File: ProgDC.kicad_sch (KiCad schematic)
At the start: 45 parts, among them J1 Conn_02x20_Counter_Clockwise_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, J2 Conn_01x24_Pin, J3 Conn_01x03_Pin, U1 KR580VK28, U2 628512, U3 CPU

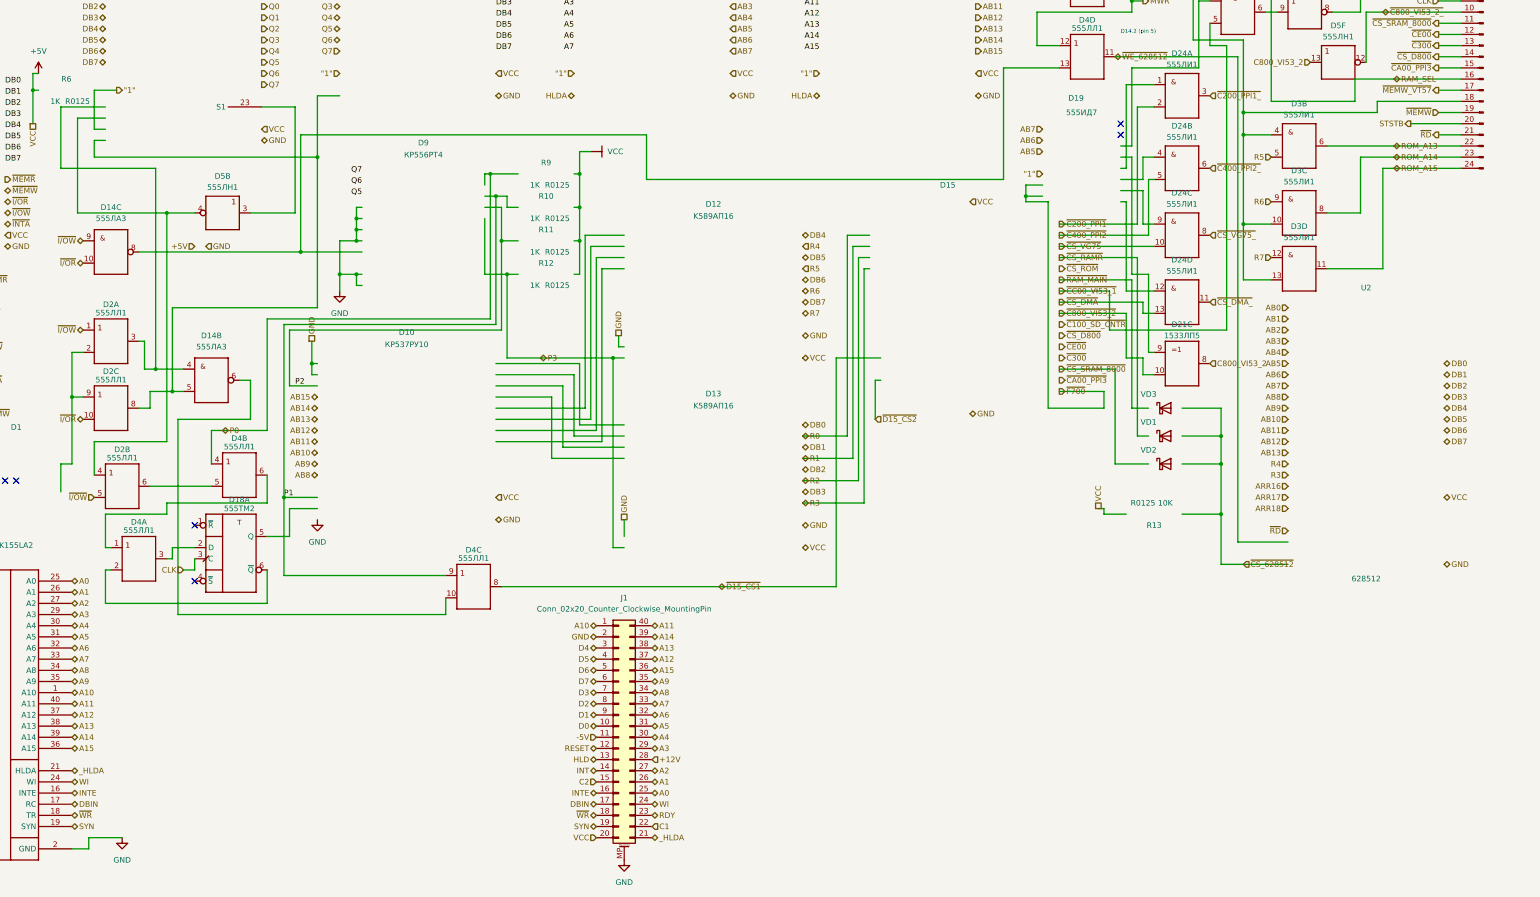
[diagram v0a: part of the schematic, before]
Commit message: Fix address and data buffering
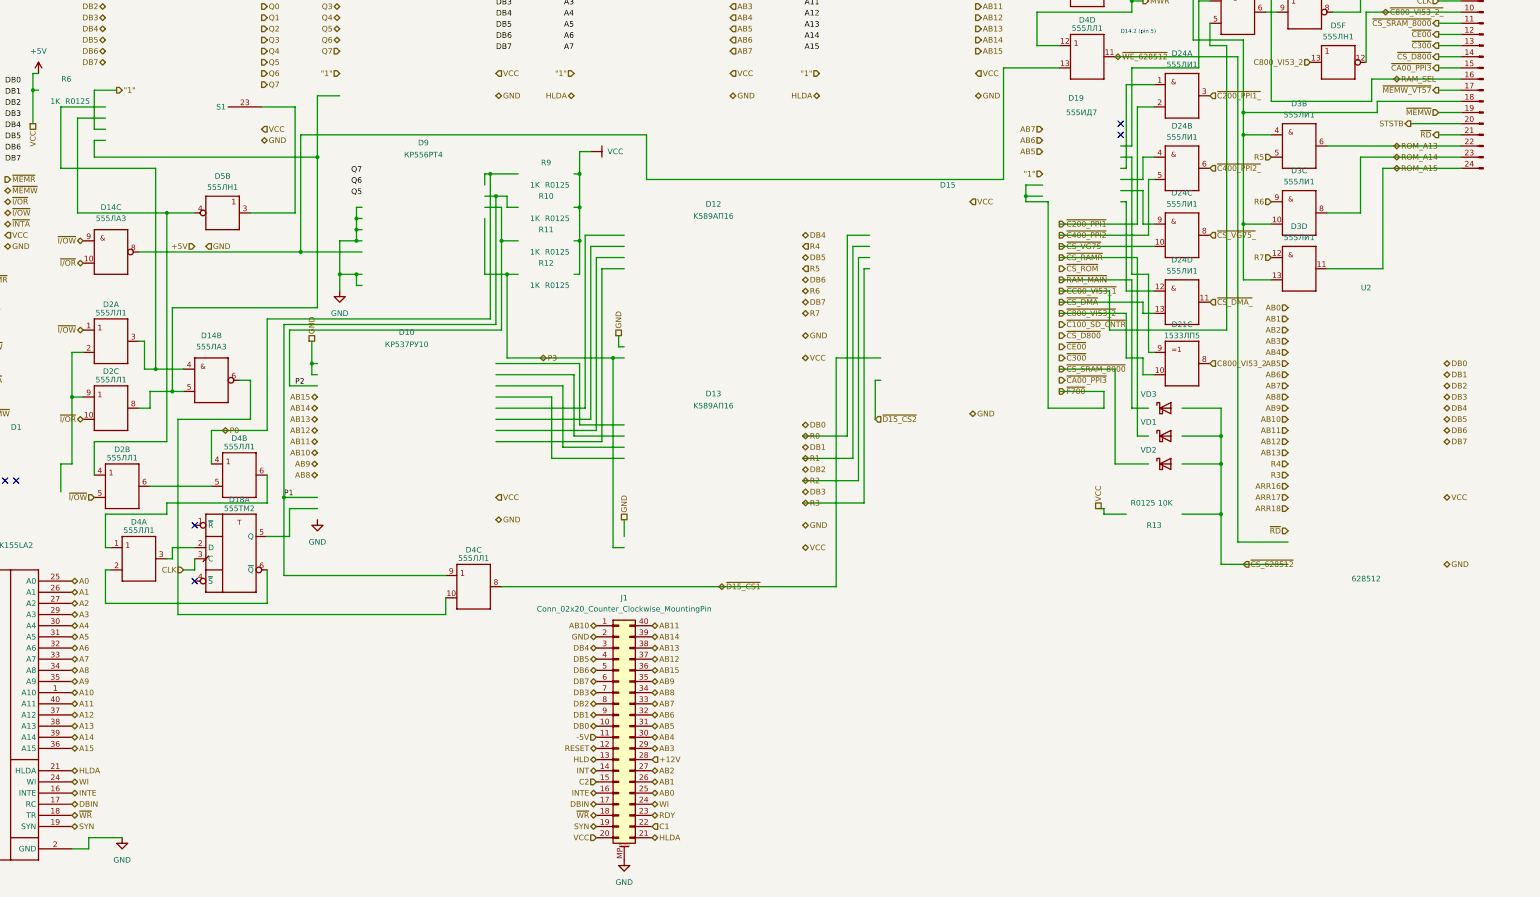
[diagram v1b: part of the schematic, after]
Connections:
- net _HLDA is gone; now on net HLDA: J1.21 (Pin_21), U3.21 (HLDA)
- net A0: no longer J1.25 (Pin_25)
- net A1: no longer J1.26 (Pin_26)
- net A10: no longer J1.1 (Pin_1)
- net A11: no longer J1.40 (Pin_40)
- net A12: no longer J1.37 (Pin_37)
- net A13: no longer J1.38 (Pin_38)
- net A14: no longer J1.39 (Pin_39)
- net A15: no longer J1.36 (Pin_36)
- net A2: no longer J1.27 (Pin_27)
- net A3: no longer J1.29 (Pin_29)
- net A4: no longer J1.30 (Pin_30)
- net A5: no longer J1.31 (Pin_31)
- net A6: no longer J1.32 (Pin_32)
- net A7: no longer J1.33 (Pin_33)
- net A8: no longer J1.34 (Pin_34)
- net A9: no longer J1.35 (Pin_35)
- net AB0: now also J1.25 (Pin_25)
- net AB1: now also J1.26 (Pin_26)
- net AB10: now also J1.1 (Pin_1)
- net AB11: now also J1.40 (Pin_40)
- net AB12: now also J1.37 (Pin_37)
- net AB13: now also J1.38 (Pin_38)
- net AB14: now also J1.39 (Pin_39)
- net AB15: now also J1.36 (Pin_36)
- net AB2: now also J1.27 (Pin_27)
- net AB3: now also J1.29 (Pin_29)
- net AB4: now also J1.30 (Pin_30)
- net AB5: now also J1.31 (Pin_31)
- net AB6: now also J1.32 (Pin_32)
- net AB7: now also J1.33 (Pin_33)
- net AB8: now also J1.34 (Pin_34)
- net AB9: now also J1.35 (Pin_35)
- net D0: no longer J1.10 (Pin_10)
- net D1: no longer J1.9 (Pin_9)
- net D2: no longer J1.8 (Pin_8)
- net D3: no longer J1.7 (Pin_7)
- net D4: no longer J1.3 (Pin_3)
- net D5: no longer J1.4 (Pin_4)
- net D6: no longer J1.5 (Pin_5)
- net D7: no longer J1.6 (Pin_6)
- net DB0: now also J1.10 (Pin_10)
- net DB1: now also J1.9 (Pin_9)
- net DB2: now also J1.8 (Pin_8)
- net DB3: now also J1.7 (Pin_7)
- net DB4: now also J1.3 (Pin_3)
- net DB5: now also J1.4 (Pin_4)
- net DB6: now also J1.5 (Pin_5)
- net DB7: now also J1.6 (Pin_6)
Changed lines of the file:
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@@
 	(wire
 		(pts
-			(xy 375.92 109.22) (xy 375.92 104.14)
+			(xy 379.73 109.22) (xy 379.73 104.14)
 		)
 		(stroke
@@
 	(wire
 		(pts
-			(xy 375.92 104.14) (xy 400.05 104.14)
+			(xy 379.73 104.14) (xy 400.05 104.14)
 		)
 		(stroke
@@
 	(wire
 		(pts
-			(xy 356.87 109.22) (xy 375.92 109.22)
+			(xy 356.87 109.22) (xy 379.73 109.22)
 		)
 		(stroke
@@
 		)
 	)
-	(hierarchical_label "_HLDA"
+	(hierarchical_label "HLDA"
 		(shape bidirectional)
 		(at 83.82 261.62 0)
@@
 				(size 1.27 1.27)
 			)
-			(justify left)
+			(justify left bottom)
 		)
 	)
@@
 		)
 	)
-	(hierarchical_label "D4"
+	(hierarchical_label "DB4"
 		(shape bidirectional)
 		(at 203.2 233.68 180)
@@
 				(size 1.27 1.27)
 			)
-			(justify left)
+			(justify left bottom)
 		)
 	)
@@
 		)
 	)
-	(hierarchical_label "A0"
+	(hierarchical_label "AB0"
 		(shape bidirectional)
 		(at 215.9 266.7 0)
@@
 				(size 1.27 1.27)
 			)
-			(justify left)
+			(justify left bottom)
 		)
 	)
@@
 		)
 	)
-	(hierarchical_label "A10"
+	(hierarchical_label "AB10"
 		(shape bidirectional)
 		(at 203.2 228.6 180)
@@
 		)
 	)
-	(hierarchical_label "D6"
+	(hierarchical_label "DB6"
 		(shape bidirectional)
 		(at 203.2 238.76 180)
@@
 		)
 	)
-	(hierarchical_label "_HLDA"
+	(hierarchical_label "HLDA"
 		(shape bidirectional)
 		(at 215.9 276.86 0)
@@
 		)
 	)
-	(hierarchical_label "D5"
+	(hierarchical_label "DB5"
 		(shape bidirectional)
 		(at 203.2 236.22 180)
@@
 				(size 1.27 1.27)
 			)
-			(justify left)
+			(justify left bottom)
 		)
 	)
@@
 				(size 1.27 1.27)
 			)
-			(justify left)
+			(justify left bottom)
 		)
 	)
@@
 		)
 	)
-	(hierarchical_label "A13"
+	(hierarchical_label "AB13"
 		(shape bidirectional)
 		(at 215.9 233.68 0)
@@
 				(size 1.27 1.27)
 			)
-			(justify left)
+			(justify left bottom)
 		)
 	)
@@
 		)
 	)
-	(hierarchical_label "D0"
+	(hierarchical_label "DB0"
 		(shape bidirectional)
 		(at 203.2 251.46 180)
@@
 		)
 	)
-	(hierarchical_label "A14"
+	(hierarchical_label "AB14"
 		(shape bidirectional)
 		(at 215.9 231.14 0)
@@
 		)
 	)
-	(hierarchical_label "A9"
+	(hierarchical_label "AB9"
 		(shape bidirectional)
 		(at 215.9 241.3 0)
@@
 		)
 	)
-	(hierarchical_label "A5"
+	(hierarchical_label "AB5"
 		(shape bidirectional)
 		(at 215.9 251.46 0)
@@
 				(size 1.27 1.27)
 			)
-			(justify left)
+			(justify left bottom)
 		)
 	)
-	(hierarchical_label "D7"
+	(hierarchical_label "DB7"
 		(shape bidirectional)
 		(at 203.2 241.3 180)
@@
 				(size 1.27 1.27)
 			)
-			(justify left)
+			(justify left bottom)
 		)
 	)
@@
 		)
 	)
-	(hierarchical_label "A4"
+	(hierarchical_label "AB4"
 		(shape bidirectional)
 		(at 215.9 254 0)
@@
 		)
 	)
-	(hierarchical_label "A1"
+	(hierarchical_label "AB1"
 		(shape bidirectional)
 		(at 215.9 264.16 0)
@@
 				(size 1.27 1.27)
 			)
-			(justify left)
+			(justify left bottom)
 		)
 	)
@@
 				(size 1.27 1.27)
 			)
-			(justify left)
+			(justify left bottom)
 		)
 	)
@@
 		)
 	)
-	(hierarchical_label "D1"
+	(hierarchical_label "DB1"
 		(shape bidirectional)
 		(at 203.2 248.92 180)
@@
 		)
 	)
-	(hierarchical_label "A15"
+	(hierarchical_label "AB15"
 		(shape bidirectional)
 		(at 215.9 238.76 0)
@@
 				(size 1.27 1.27)
 			)
-			(justify left)
+			(justify left bottom)
 		)
 	)
@@
 				(size 1.27 1.27)
 			)
-			(justify left)
+			(justify left bottom)
 		)
 	)
@@
 				(size 1.27 1.27)
 			)
-			(justify left)
+			(justify left bottom)
 		)
 	)
@@
 		)
 	)
-	(hierarchical_label "A7"
+	(hierarchical_label "AB7"
 		(shape bidirectional)
 		(at 215.9 246.38 0)
@@
 				(size 1.27 1.27)
 			)
-			(justify left)
+			(justify left bottom)
 		)
 	)
@@
 				(size 1.27 1.27)
 			)
-			(justify left)
+			(justify left bottom)
 		)
 	)
@@
 		)
 	)
-	(hierarchical_label "A2"
+	(hierarchical_label "AB2"
 		(shape bidirectional)
 		(at 215.9 261.62 0)
@@
 		)
 	)
-	(hierarchical_label "A3"
+	(hierarchical_label "AB3"
 		(shape bidirectional)
 		(at 215.9 256.54 0)
@@
 		)
 	)
-	(hierarchical_label "A6"
+	(hierarchical_label "AB6"
 		(shape bidirectional)
 		(at 215.9 248.92 0)
@@
 				(size 1.27 1.27)
 			)
-			(justify left)
+			(justify left bottom)
 		)
 	)
@@
 		)
 	)
-	(hierarchical_label "A11"
+	(hierarchical_label "AB11"
 		(shape bidirectional)
 		(at 215.9 228.6 0)
@@
 				(size 1.27 1.27)
 			)
-			(justify left)
+			(justify left bottom)
 		)
 	)
@@
 		)
 	)
-	(hierarchical_label "A8"
+	(hierarchical_label "AB8"
 		(shape bidirectional)
 		(at 215.9 243.84 0)
@@
 		)
 	)
-	(hierarchical_label "D3"
+	(hierarchical_label "DB3"
 		(shape bidirectional)
 		(at 203.2 243.84 180)
@@
 				(size 1.27 1.27)
 			)
-			(justify left)
+			(justify left bottom)
 		)
 	)
@@
 		)
 	)
-	(hierarchical_label "D2"
+	(hierarchical_label "DB2"
 		(shape bidirectional)
 		(at 203.2 246.38 180)
@@
 				(size 1.27 1.27)
 			)
-			(justify right)
+			(justify right bottom)
 		)
 	)
@@
 		)
 	)
-	(hierarchical_label "A12"
+	(hierarchical_label "AB12"
 		(shape bidirectional)
 		(at 215.9 236.22 0)

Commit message: Ver. 1.4
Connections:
- net ~{CS_DMA_}: now also D22.9 (A); no longer J2.8 (Pin_8)
- net ~{CS_RAMR}: now also D22.5 (A)
- net ~{WR}: now also D22.1 (A)
- net ~{CS_DMA_2}: now reaches D21.11 (Y)
- net ~{CS_DMA_2}: now also J2.8 (Pin_8)
- net at D21.12 (A): now also D22.8 (Y)
- net at D21.13 (B): now also D14.11 (Y)
- net at D22.2 (Y): now also D14.12 (A)
- net at D22.6 (Y): now also D14.13 (B)
- no-connect marks 22 -> 10
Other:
- moved on the sheet: D14D, D21D, D22A, D22C, D22D

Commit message: Fix
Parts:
- added C1: 470, Capacitor_THT:C_Disc_D3.0mm_W1.6mm_P2.50mm, symbol Device:C_Small
- added D16: 133LL1, Package_DIP:DIP-14_W7.62mm, symbol Pico-altium-import:root_0_133LL1_*
- added R14: R0125, Resistor_THT:R_Axial_DIN0204_L3.6mm_D1.6mm_P2.54mm_Vertical, symbol Pico-altium-import:root_2_R0125_*
- added VD4, VD5: 1N4148, Diode_THT:D_DO-34_SOD68_P2.54mm_Vertical_AnodeUp, symbol Diode:BAT43
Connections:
- net +5V: now also D16.14 (VCC), D16.14 (VCC), D16.14 (VCC), D16.14 (VCC), R14.2 (BOT)
- net GND: now also D21.12 (A), C1.2, D16.7 (GND), D16.7 (GND), D16.7 (GND), D16.7 (GND)
- net ~{CS_628512}: now also C1.1, D16.2 (B)
- net ~{CS_DMA_}: no longer D22.9 (A)
- net ~{CS_RAMR}: now also D16.10 (B)
- net ~{WE_628512}: now also D16.1 (A)
- net ~{WR}: now also D16.9 (A); no longer D22.1 (A)
- net at D22.8 (Y): no longer D21.12 (A)
- net at D14.11 (Y): no longer D21.13 (B)
- net at D14.12 (A): no longer D22.2 (Y)
- net at D14.13 (B): no longer D22.6 (Y)
- net at D14.8 (Y): now also D16.13 (B); no longer D4.13 (B)
- new net: D21.13 (B), R14.1 (TOP)
- new net: D16.11 (Y), D4.13 (B)
- new net CS_RAMR: D16.12 (A), D22.6 (Y)
- no-connect marks 10 -> 20
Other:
- moved on the sheet: D3C, D3D, VD1, VD3

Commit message: Update PCB
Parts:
- added D17: КР1533КП11, Package_DIP:DIP-16_W7.62mm, symbol Pico-altium-import:root_0_KR1533KP11_*
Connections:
- net +5V: now also D17.16 (VCC)
- net GND: now also D17.15 (~{OE}), D17.8 (GND)
- net P3: now also D17.1 (SEL)
- net Q1: now also D17.6 (2B)
- net Q2: now also D17.10 (3B)
- net Q3: now also D17.5 (2A)
- net Q4: now also D17.11 (3A)
- no-connect marks 20 -> 26
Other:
- note added: "BLUE"
- note added: "RED"
- note added: "YELLOW"
- moved on the sheet: D14B, D14C, D18A, D4A, D4C, D5B

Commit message: Fix bugs
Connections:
- net ~{A_FF}: now reaches D2.2 (B), D2.9 (A)
- net ~{CA00_PPI3} renamed ~{C500_VDP}
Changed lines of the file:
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@@
 	(title_block
 		(title "Программируемый дешифратор Пальмира")
-		(date "2025-04-10")
+		(date "2026-03-16")
+		(rev "1.5")
+		(comment 1 "1.5")
 		(comment 2 "Цветков Д.С.")
-		(comment 3 "1")
-		(comment 4 "2")
 		(comment 5 "3")
 		(comment 6 "4")
@@
 		)
 	)
-	(text_box "Программируемый дешифратор Пальмира\n                               Ver 1.4\n"
+	(text_box "Программируемый дешифратор Пальмира\n                               Ver 1.5\n"
 		(exclude_from_sim no)
 		(at 274.505 46.276 0)
@@
 		(stroke
 			(width -0.0001)
-			(type default)
+			(type solid)
 			(color 0 0 0 1)
 		)
@@
 	(hierarchical_label "GND"
 		(shape bidirectional)
-		(at 180.34 205.74 0)
+		(at 189.23 205.74 0)
 		(effects
 			(font
@@
 		)
 	)
-	(hierarchical_label "~{CA00_PPI3}"
+	(hierarchical_label "~{C500_VDP}"
 		(shape output)
 		(at 394.97 101.6 180)
@@
 		)
 	)
-	(hierarchical_label "~{CA00_PPI3}"
+	(hierarchical_label "~{C500_VDP}"
 		(shape output)
 		(at 308.61 172.72 0)
@@
 	(hierarchical_label "VCC"
 		(shape input)
-		(at 180.34 200.66 0)
+		(at 189.23 200.66 0)
 		(effects
 			(font
@@
 		)
 	)
+	(hierarchical_label "~{A_FF}"
+		(shape bidirectional)
+		(at 77.47 176.53 0)
+		(effects
+			(font
+				(size 1.27 1.27)
+			)
+			(justify left bottom)
+		)
+	)

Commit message: Fix bugs
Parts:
- removed D23: 555TM2, Package_DIP:DIP-14_W7.62mm, symbol Pico-altium-import:root_0_133TM2_*
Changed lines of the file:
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@@
-	)
-	(symbol
-		(lib_id "Pico-altium-import:root_0_133TM2_*")
-		(at 146.05 45.72 0)
-		(unit 2)
-		(exclude_from_sim no)
-		(in_bom yes)
-		(on_board yes)
-		(dnp no)
-		(fields_autoplaced yes)
-		(property "Reference" "D23"
-			(at 153.9875 38.1 0)
-			(effects
-				(font
-					(size 1.27 1.27)
-				)
-			)
-		)
-		(property "Value" "555TM2"
-			(at 153.9875 40.64 0)
-			(effects
-				(font
-					(size 1.27 1.27)
-				)
-			)
-		)
-		(property "Footprint" "Package_DIP:DIP-14_W7.62mm"
-			(at 146.05 45.72 0)
-			(effects
-				(font
-					(size 1.27 1.27)
-				)
-				(hide yes)
-			)
-		)
-		(property "Datasheet" ""
-			(at 146.05 45.72 0)
-			(effects
-				(font
-					(size 1.27 1.27)
-				)
-				(hide yes)
-			)
-		)
-		(property "Description" "133TM2"
-			(at 146.05 45.72 0)
-			(effects
-				(font
-					(size 1.27 1.27)
-				)
-				(hide yes)
-			)
-		)
-		(property "ALTIUM_VALUE" ""
-			(at 155.575 52.07 90)
-			(effects
-				(font
-					(size 1.27 1.27)
-				)
-				(hide yes)
-			)
-		)
-		(pin "11"
-		)
-		(pin "14"
-		)
-		(pin "7"
-		)
-		(pin "2"
-		)
-		(pin "3"
-		)
-		(pin "4"
-		)
-		(pin "5"
-		)
-		(pin "6"
-		)
-		(pin "13"
-		)
-		(pin "1"
-		)
-		(pin "12"
-		)
-		(pin "10"
-		)
-		(pin "9"
-		)
-		(pin "8"
-		)
-		(instances
-			(project ""
-				(path "/1c1c0805-b5d6-4e37-a393-ae6b53285b27"
-					(reference "D23")
-					(unit 2)
-				)
-			)
-		)
 	)
 	(symbol
@@
 				)
 			)
-		)
-	)
-	(symbol
-		(lib_id "Pico-altium-import:root_0_133TM2_*")
-		(at 121.92 45.72 0)
-		(unit 1)
-		(exclude_from_sim no)
-		(in_bom yes)
-		(on_board yes)
-		(dnp no)
-		(fields_autoplaced yes)
-		(property "Reference" "D23"
-			(at 129.8575 38.1 0)
-			(effects
-				(font
-					(size 1.27 1.27)
-				)
-			)
-		)
-		(property "Value" "555TM2"
-			(at 129.8575 40.64 0)
-			(effects
-				(font
-					(size 1.27 1.27)
-				)
-			)
-		)
-		(property "Footprint" "Package_DIP:DIP-14_W7.62mm"
-			(at 121.92 45.72 0)
-			(effects
-				(font
-					(size 1.27 1.27)
-				)
-				(hide yes)
-			)
-		)
-		(property "Datasheet" ""
-			(at 121.92 45.72 0)
-			(effects
-				(font
-					(size 1.27 1.27)
-				)
-				(hide yes)
-			)
-		)
-		(property "Description" "133TM2"
-			(at 121.92 45.72 0)
-			(effects
-				(font
-					(size 1.27 1.27)
-				)
-				(hide yes)
-			)
-		)
-		(property "ALTIUM_VALUE" ""
-			(at 131.445 52.07 90)
-			(effects
-				(font
-					(size 1.27 1.27)
-				)
-				(hide yes)
-			)
-		)
-		(pin "7"
-		)
-		(pin "13"
-		)
-		(pin "3"
-		)
-		(pin "12"
-		)
-		(pin "9"
-		)
-		(pin "2"
-		)
-		(pin "11"
-		)
-		(pin "10"
-		)
-		(pin "4"
-		)
-		(pin "6"
-		)
-		(pin "8"
-		)
-		(pin "14"
-		)
-		(pin "1"
-		)
-		(pin "5"
-		)
-		(instances
-			(project ""
-				(path "/1c1c0805-b5d6-4e37-a393-ae6b53285b27"
-					(reference "D23")
-					(unit 1)
-				)
-			)

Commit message: Fix bugs
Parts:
- D10: value КР537РУ10 -> 6116SA45P
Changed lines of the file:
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@@
 	)
 	(junction
+		(at 148.59 135.89)
+		(diameter 0)
+		(color 0 0 0 0)
+	)
+	(junction
 		(at 139.7 200.66)
 		(diameter 0)
@@
 	)
 	(junction
-		(at 148.59 143.51)
-		(diameter 0)
-		(color 0 0 0 0)
-	)
-	(junction
 		(at 181.61 140.97)
 		(diameter 0)
@@
 	(wire
 		(pts
-			(xy 148.59 143.51) (xy 148.59 148.59)
-		)
-		(stroke
-			(width 0)
-			(type default)
-		)
-	)
-	(wire
-		(pts
 			(xy 262.89 144.78) (xy 265.43 144.78)
 		)
@@
 	(wire
 		(pts
-			(xy 148.59 140.97) (xy 148.59 143.51)
+			(xy 148.59 140.97) (xy 148.59 148.59)
 		)
 		(stroke
@@
 	(wire
 		(pts
-			(xy 146.05 133.35) (xy 149.86 133.35)
-		)
-		(stroke
-			(width 0)
-			(type default)
-		)
-	)
-	(wire
-		(pts
 			(xy 97.79 143.51) (xy 95.25 143.51)
 		)
@@
 	(wire
 		(pts
+			(xy 146.05 143.51) (xy 149.86 143.51)
+		)
+		(stroke
+			(width 0)
+			(type default)
+		)
+	)
+	(wire
+		(pts
 			(xy 336.55 191.77) (xy 345.44 191.77)
 		)
@@
 	(wire
 		(pts
-			(xy 148.59 143.51) (xy 149.86 143.51)
-		)
-		(stroke
-			(width 0)
-			(type default)
-		)
-	)
-	(wire
-		(pts
 			(xy 257.81 30.48) (xy 232.41 30.48)
 		)
@@
 	(wire
 		(pts
+			(xy 149.86 133.35) (xy 148.59 133.35)
+		)
+		(stroke
+			(width 0)
+			(type default)
+		)
+	)
+	(wire
+		(pts
 			(xy 204.47 53.34) (xy 204.47 59.69)
 		)
@@
 	(wire
 		(pts
-			(xy 146.05 133.35) (xy 146.05 132.08)
-		)
-		(stroke
-			(width 0)
-			(type default)
-		)
-	)
-	(wire
-		(pts
 			(xy 81.28 193.04) (xy 81.28 198.12)
 		)
@@
 	(wire
 		(pts
+			(xy 148.59 133.35) (xy 148.59 135.89)
+		)
+		(stroke
+			(width 0)
+			(type default)
+		)
+	)
+	(wire
+		(pts
 			(xy 381 111.76) (xy 381 109.22)
 		)
@@
 	(wire
 		(pts
+			(xy 146.05 132.08) (xy 146.05 143.51)
+		)
+		(stroke
+			(width 0)
+			(type default)
+		)
+	)
+	(wire
+		(pts
 			(xy 91.44 118.11) (xy 90.17 118.11)
 		)
@@
 			)
 		)
-		(property "Value" "КР537РУ10"
+		(property "Value" "6116SA45P"
 			(at 166.37 159.512 0)
 			(effects

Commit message: Add PSG select
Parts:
- added D23: 555TM2, Package_DIP:DIP-14_W7.62mm, symbol Pico-altium-import:root_0_133TM2_*
- added R15: R0125, Resistor_THT:R_Axial_DIN0204_L3.6mm_D1.6mm_P2.54mm_Vertical, symbol Pico-altium-import:root_2_R0125_*
- added VD6, VD7: 1N4148, Diode_THT:D_DO-34_SOD68_P2.54mm_Vertical_AnodeUp, symbol Diode:BAT43
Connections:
- net +5V: now also D23.14 (VCC), D23.14 (VCC), R15.2 (BOT)
- net 8MHZ: now also D23.11 (C), D23.5 (Q)
- net C800_VI53_2: no longer D21.8 (Y)
- net CLK: now also D23.9 (Q)
- net GND: now also D21.10 (B), D23.7 (GND), D23.7 (GND)
- net Q0: now also D16.5 (B), D22.9 (A)
- net ~{C800_VI53_2}: now also D16.6 (Y); no longer D21.10 (B)
- net ~{RAM_MAIN}: no longer J2.6 (Pin_6)
- net ~{CS_PSG}: now reaches D14.11 (Y)
- net ~{CS_PSG}: now also J2.6 (Pin_6)
- net at D14.12 (A): now also D22.2 (Y)
- net at D14.13 (B): now also D22.8 (Y)
- net at D21.9 (A): now also R15.1 (TOP)
- net at D22.1 (A): now also D16.4 (A), D21.8 (Y)
- net at D22.10 (Y): now also D23.3 (C)
- new net: D23.1 (~{R}), D23.10 (~{S}), D23.13 (~{R}), D23.4 (~{S})
- new net: D23.12 (D), D23.8 (~{Q})
- new net: D23.2 (D), D23.6 (~{Q})
- no-connect marks 26 -> 16
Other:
- moved on the sheet: C1, D16A, D21C, D22C, R14, VD1, VD2, VD3
